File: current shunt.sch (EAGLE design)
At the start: 46 parts, among them Q1 BC846,215, Q2 TIP29A, Q3 BC846,215, Q4 TIP29A

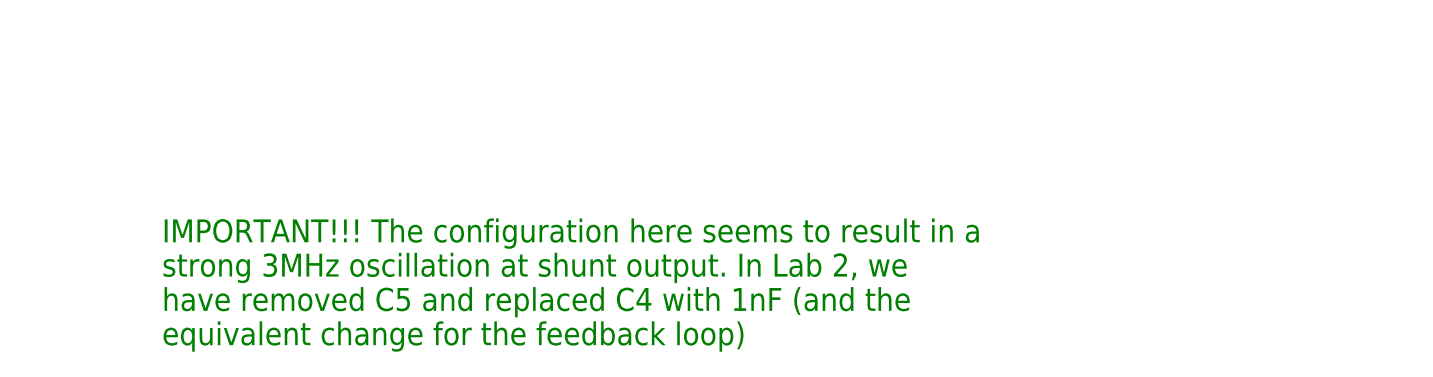
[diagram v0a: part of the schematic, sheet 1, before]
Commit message: update schematics to the version that was used for measurements in https://arxiv.org/abs/1808.03310
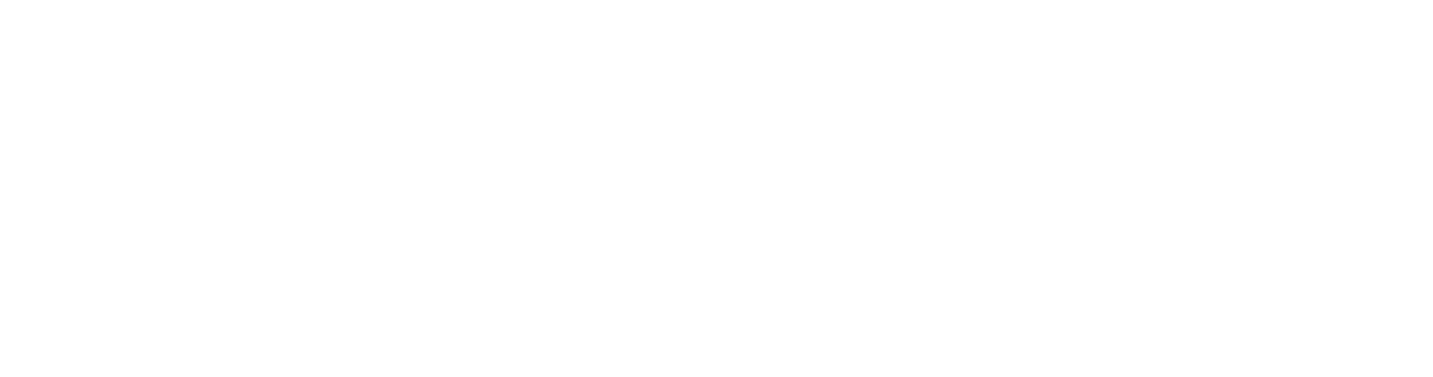
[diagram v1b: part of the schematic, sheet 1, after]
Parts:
- R9: value 20k -> 30k
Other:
- note added: "I_shunt = 1 A/V * V_FB_SHUNT = 0.03 A/V * V_FB_SIG"
- note removed: "IMPORTANT!!! The configuration here seems to result in a strong 3MHz oscillation at shunt output. In Lab 2, we have removed C5 and replaced C4 with 1nF (and the equivalent change for the feedback loop)"
- note removed: "I_shunt = 1 A/V * V_FF_SHUNT = 0.05 A/V * V_FF_SIG"
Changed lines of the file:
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@@
 <?xml version="1.0" encoding="utf-8"?>
 <!DOCTYPE eagle SYSTEM "eagle.dtd">
-<eagle version="6.6.0">
+<eagle version="8.3.2">
 <drawing>
 <settings>
 <setting alwaysvectorfont="no"/>
+<setting keepoldvectorfont="yes"/>
 <setting verticaltext="up"/>
 </settings>
@@
 <part name="SIG+PWR" library="custom-con" deviceset="MOLEX-KK-1X5" device=""/>
 <part name="R10" library="custom-passive" deviceset="RES" device="0603" value="1k"/>
-<part name="R9" library="custom-passive" deviceset="RES" device="0603" value="20k"/>
+<part name="R9" library="custom-passive" deviceset="RES" device="0603" value="30k"/>
 <part name="GND6" library="supply1" deviceset="GND" device=""/>
 <part name="R11" library="custom-passive" deviceset="RES" device="0603" value="1k"/>
@@
 <text x="203.2" y="30.48" size="1.778" layer="98">I_shunt = 0.1 A/V * V_FF_SHUNT
         = 0.01 A/V * V_FF_SIG</text>
-<text x="33.02" y="22.86" size="2.54" layer="91">IMPORTANT!!! The configuration here seems to result in a
-strong 3MHz oscillation at shunt output. In Lab 2, we
-have removed C5 and replaced C4 with 1nF (and the
-equivalent change for the feedback loop)</text>
 </plain>
 <instances>
@@
 <wire x1="218.44" y1="137.16" x2="71.12" y2="137.16" width="0.508" layer="98" style="longdash"/>
 <text x="76.2" y="132.08" size="1.778" layer="98">Voltage follower opamp circuit</text>
-<text x="198.12" y="12.7" size="1.778" layer="98">I_shunt = 1 A/V * V_FF_SHUNT
-        = 0.05 A/V * V_FF_SIG</text>
+<text x="198.12" y="12.7" size="1.778" layer="98">I_shunt = 1 A/V * V_FB_SHUNT
+        = 0.03 A/V * V_FB_SIG</text>
 </plain>
 <instances>
